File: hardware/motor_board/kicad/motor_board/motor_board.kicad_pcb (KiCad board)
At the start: 4 copper layers, 75 x 35 mm, 237 parts, among them J1 BOOMELE_1.27-2x10P, J2 WAFER-SH1.0-6PWB, J3 WAFER-SH1.0-6PWB, J4 S5B-XH-A, Q1 HYG015N04LS1C2, Q2 HYG015N04LS1C2, Q3 HYG015N04LS1C2, Q4 HYG015N04LS1C2, Q5 HYG015N04LS1C2, Q6 HYG015N04LS1C2, Q7 HYG015N04LS1C2, Q8 HYG015N04LS1C2, U1 STM32G474RET6, U10 SN74LVC3G17DCUR, U11 TPS22945DCKR, U12 TPS22945DCKR, U13 LM74502DDFR, U14 74LVC1G17SE-7, U2 DRV8323RHRGZR, U3 DRV8316CRRGFR, U4 DRV8316CRRGFR, U5 AP2112K-3.3TRG1, U6 SN74LVC08APWR, U7 INA239AIDGSR, U8 BQ76907RGRR, U9 SN74LVC3G17DCUR

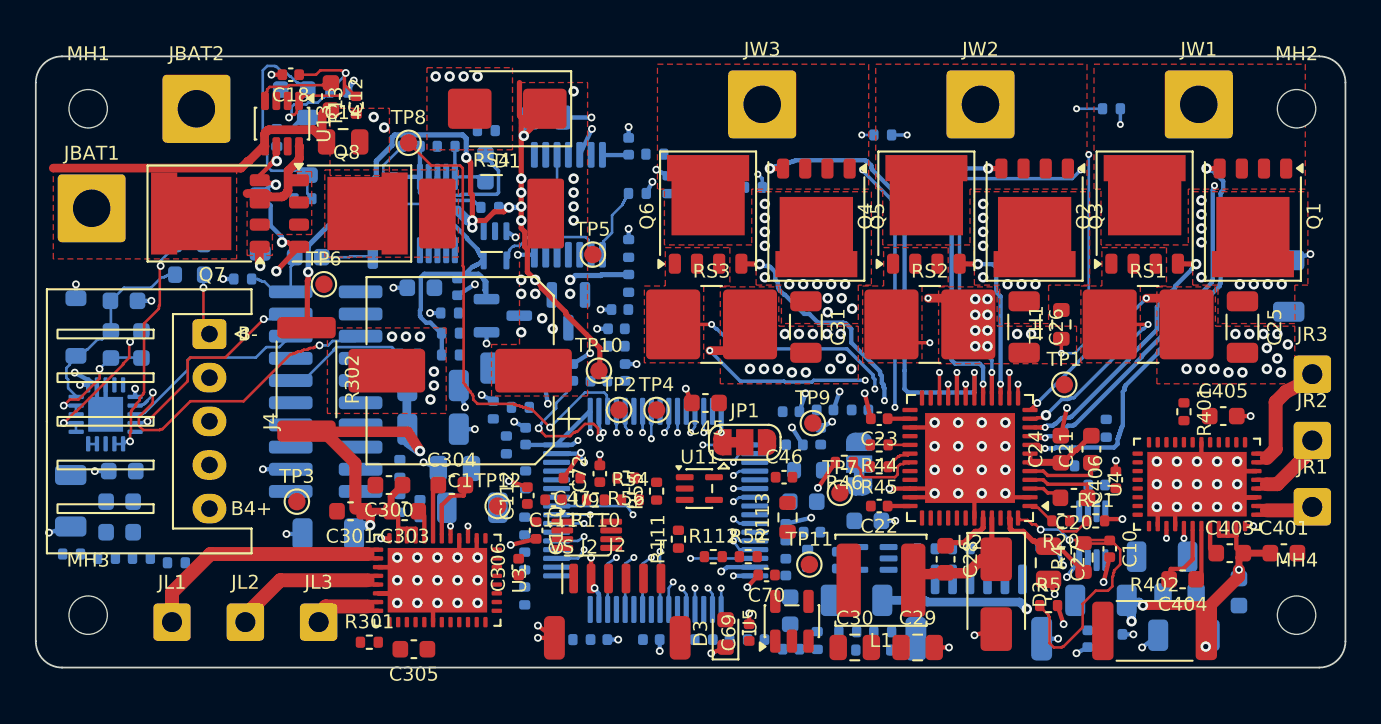
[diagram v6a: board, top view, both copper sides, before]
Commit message: motor_board routing block 7: U2/U3/U4 logic fan-out vias; router hops layers at existing own-net vias; space() sees earlier blocks' copper; greedy logic block tried and dropped (spaghetti on L3)
Co-Authored-By: Claude Opus 5.5 (1M context) <noreply@anthropic.com>
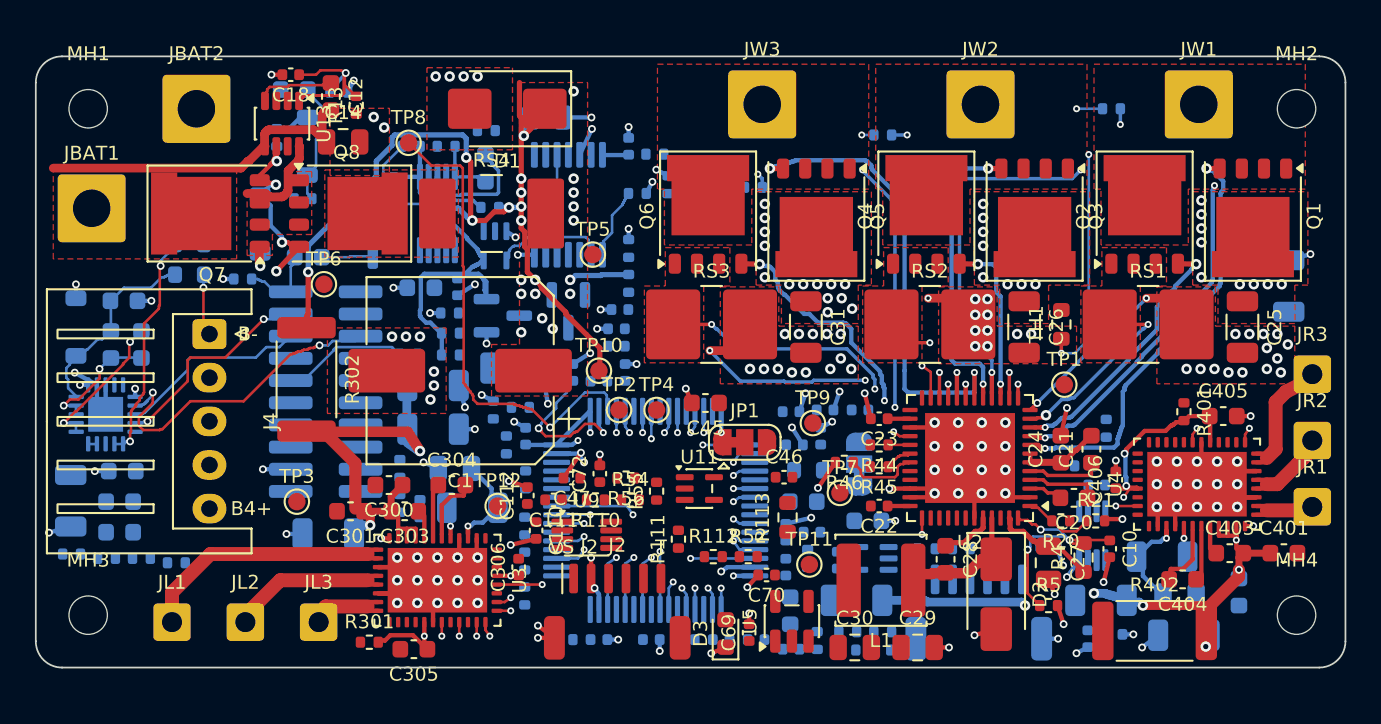
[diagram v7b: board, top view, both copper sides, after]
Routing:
- net /drive_right/R_AVDD: track 0.00 -> 12.3 mm, vias 0 -> 3
- net /drive_left/L_AVDD: track 0.00 -> 7.78 mm, vias 0 -> 2
- net /power/PSW_DV: track 12.8 -> 7.06 mm
- net /drive_right/R_FBBK: track 0.45 -> 5.92 mm
- net /drive_left/L_FBBK: track 0.45 -> 5.92 mm
- net /weapon/BUCK_EN: track 18.8 -> 13.3 mm, vias 2 -> 3
- net L_nCS: track 0.00 -> 2.60 mm, vias 0 -> 1
- net W_SOC: track 1.22 -> 3.32 mm, vias 1 -> 2
- net R_SOB: track 0.00 -> 1.25 mm, vias 0 -> 1
- net /power/PSW_EN: track 14.2 -> 15.2 mm, vias 2 -> 1
- net W_INHA: track 1.58 -> 2.51 mm, vias 1 -> 2
- net DRV_OFF: track 27.3 -> 28.2 mm, vias 1 -> 2
- net SPI_MOSI: track 0.00 -> 0.88 mm, vias 0 -> 1
- net R_INHA: track 1.31 -> 2.19 mm, vias 1 -> 2
- net +3V3: track 36.9 -> 37.8 mm, vias 4 -> 5
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
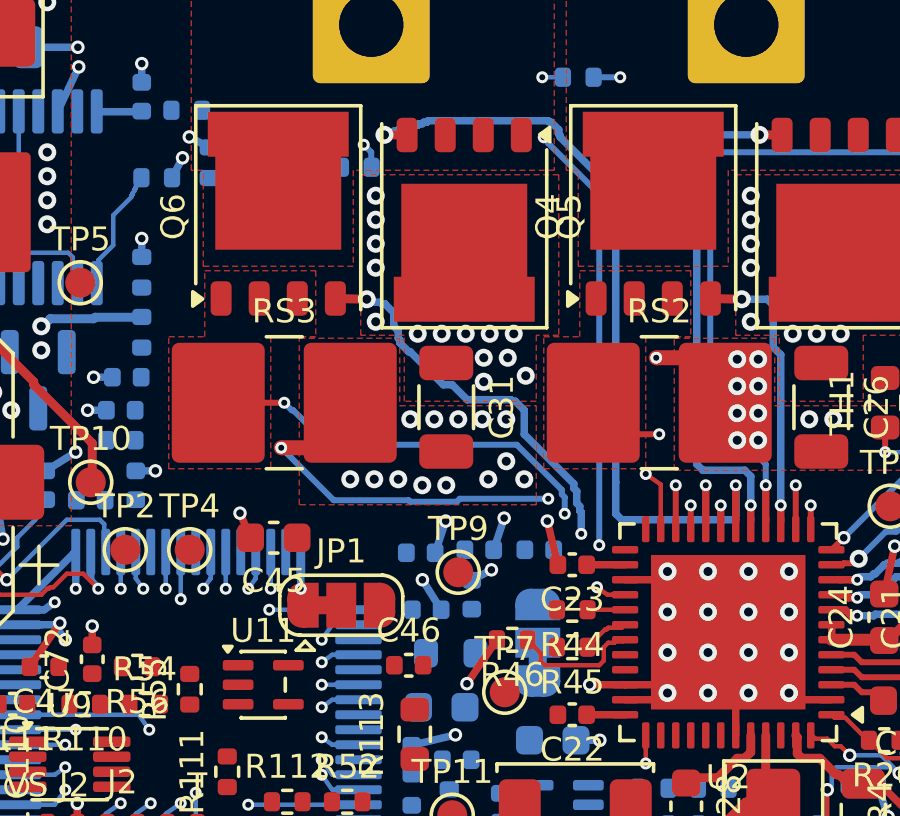
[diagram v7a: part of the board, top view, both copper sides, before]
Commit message: motor_board routing block 7b: U2 current-sense outputs (W_SOA/B/C) untangled from phase C's escape and routed to U1
SNC Kelvin lane moved to y 17.9 (stair via tucked into the VBAT feed edge), SHC stair via 0.1 west,
VREF hand-drawn, C23 0.35 mm rearward, three stitching/pad GND vias dropped (re-placed at close-out).
Tools: geo_why.py / geo_near.py (what blocks a spot, nearest legal spots), net_ends.py.

Co-Authored-By: Claude Opus 5.5 (1M context) <noreply@anthropic.com>
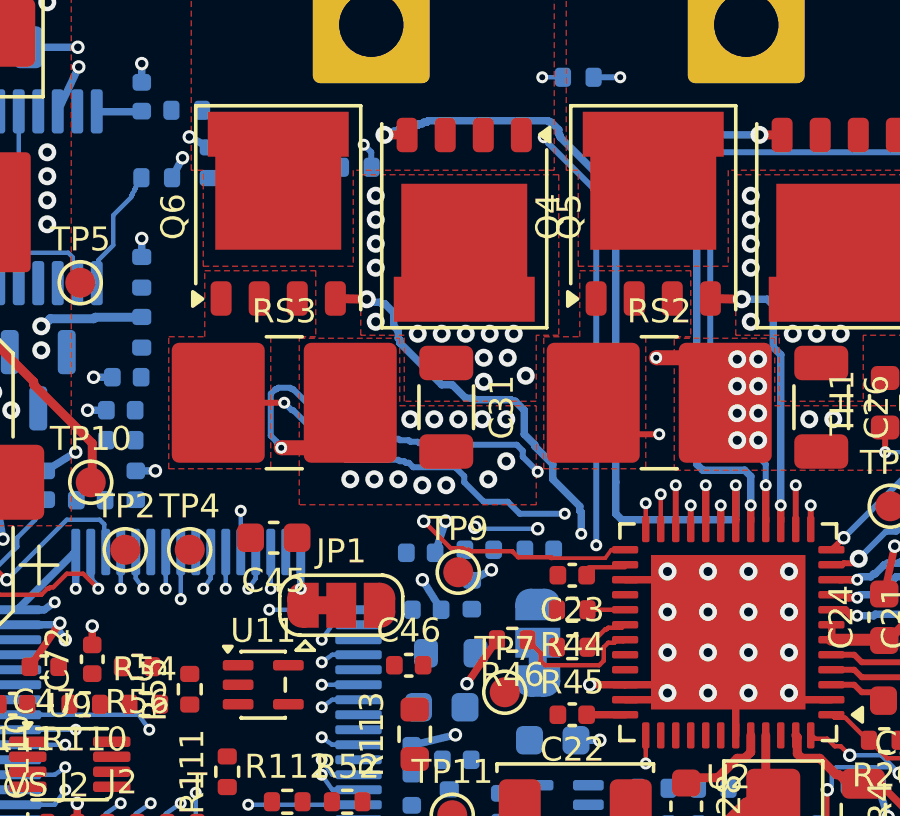
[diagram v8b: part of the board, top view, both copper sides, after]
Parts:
- moved C23 0.35 mm to (148.3, 91.1)
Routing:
- net W_SOC: track 3.32 -> 22.3 mm
- net W_SOB: track 1.31 -> 17.0 mm, vias 1 -> 4
- net W_SOA: track 0.00 -> 14.7 mm, vias 0 -> 2
- net GND: track 95.7 -> 92.2 mm, vias 172 -> 168
- net /weapon/W_SNC: track 15.3 -> 18.2 mm
- net W_nFAULT: track 11.6 -> 10.6 mm, vias 3 -> 2
